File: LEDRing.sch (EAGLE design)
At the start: 36 parts, among them U1 ATMEGA328P-AU, U2 MCP73831, U3 MIC5219 3.3V, U4 MMA8452Q, Y1 16MHZ

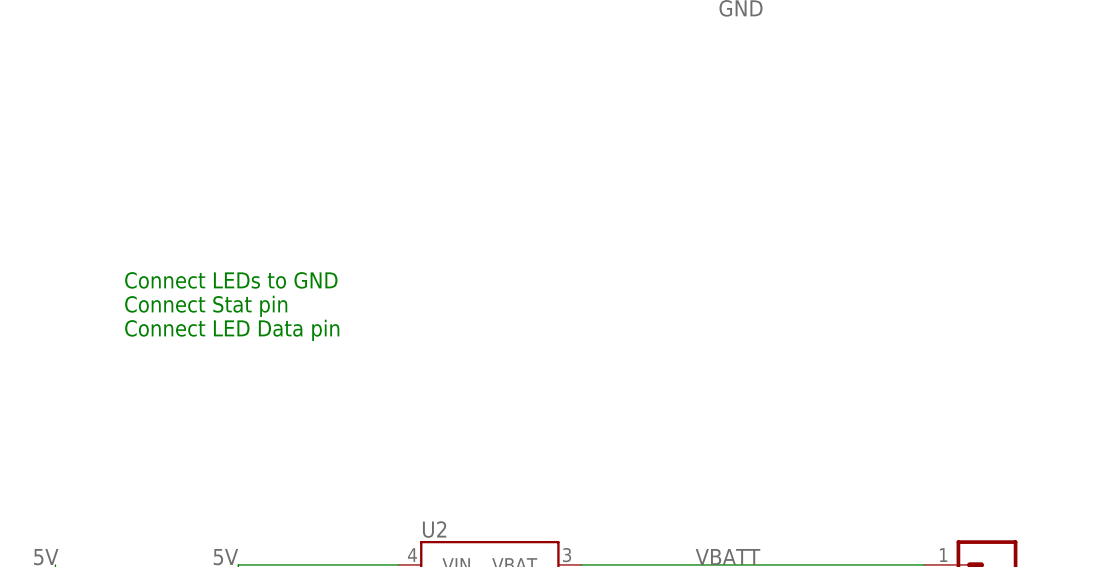
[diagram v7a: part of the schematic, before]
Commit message: Sent board to be made
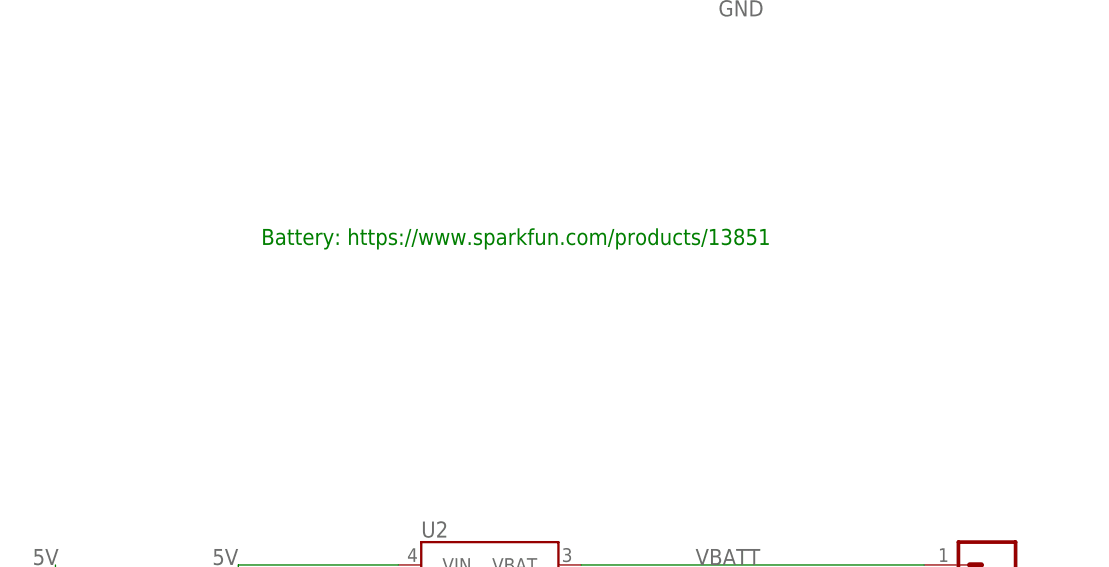
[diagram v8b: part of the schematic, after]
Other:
- note added: "Battery: https://www.sparkfun.com/products/13851"
- note removed: "Connect LEDs to GND Connect Stat pin Connect LED Data pin"
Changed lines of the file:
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@@
 <sheet>
 <plain>
-<text x="-99.06" y="15.24" size="1.778" layer="91">Connect LEDs to GND
-Connect Stat pin
-Connect LED Data pin</text>
+<text x="-83.82" y="25.4" size="1.778" layer="91">Battery: https://www.sparkfun.com/products/13851</text>
 </plain>
 <instances>
@@
 </schematic>
 </drawing>
-<compatibility>
-<note version="6.3" minversion="6.2.2" severity="warning">
-Since Version 6.2.2 text objects can contain more than one line,
-which will not be processed correctly with this version.
-</note>
-</compatibility>
 </eagle>
